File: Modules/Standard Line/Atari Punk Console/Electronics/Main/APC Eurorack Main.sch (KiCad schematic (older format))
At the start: 23 parts, among them IC1 L78L05_TO92, IC2 LM556, J1 Power, J4 CV2, J5 Out, J6 CV1

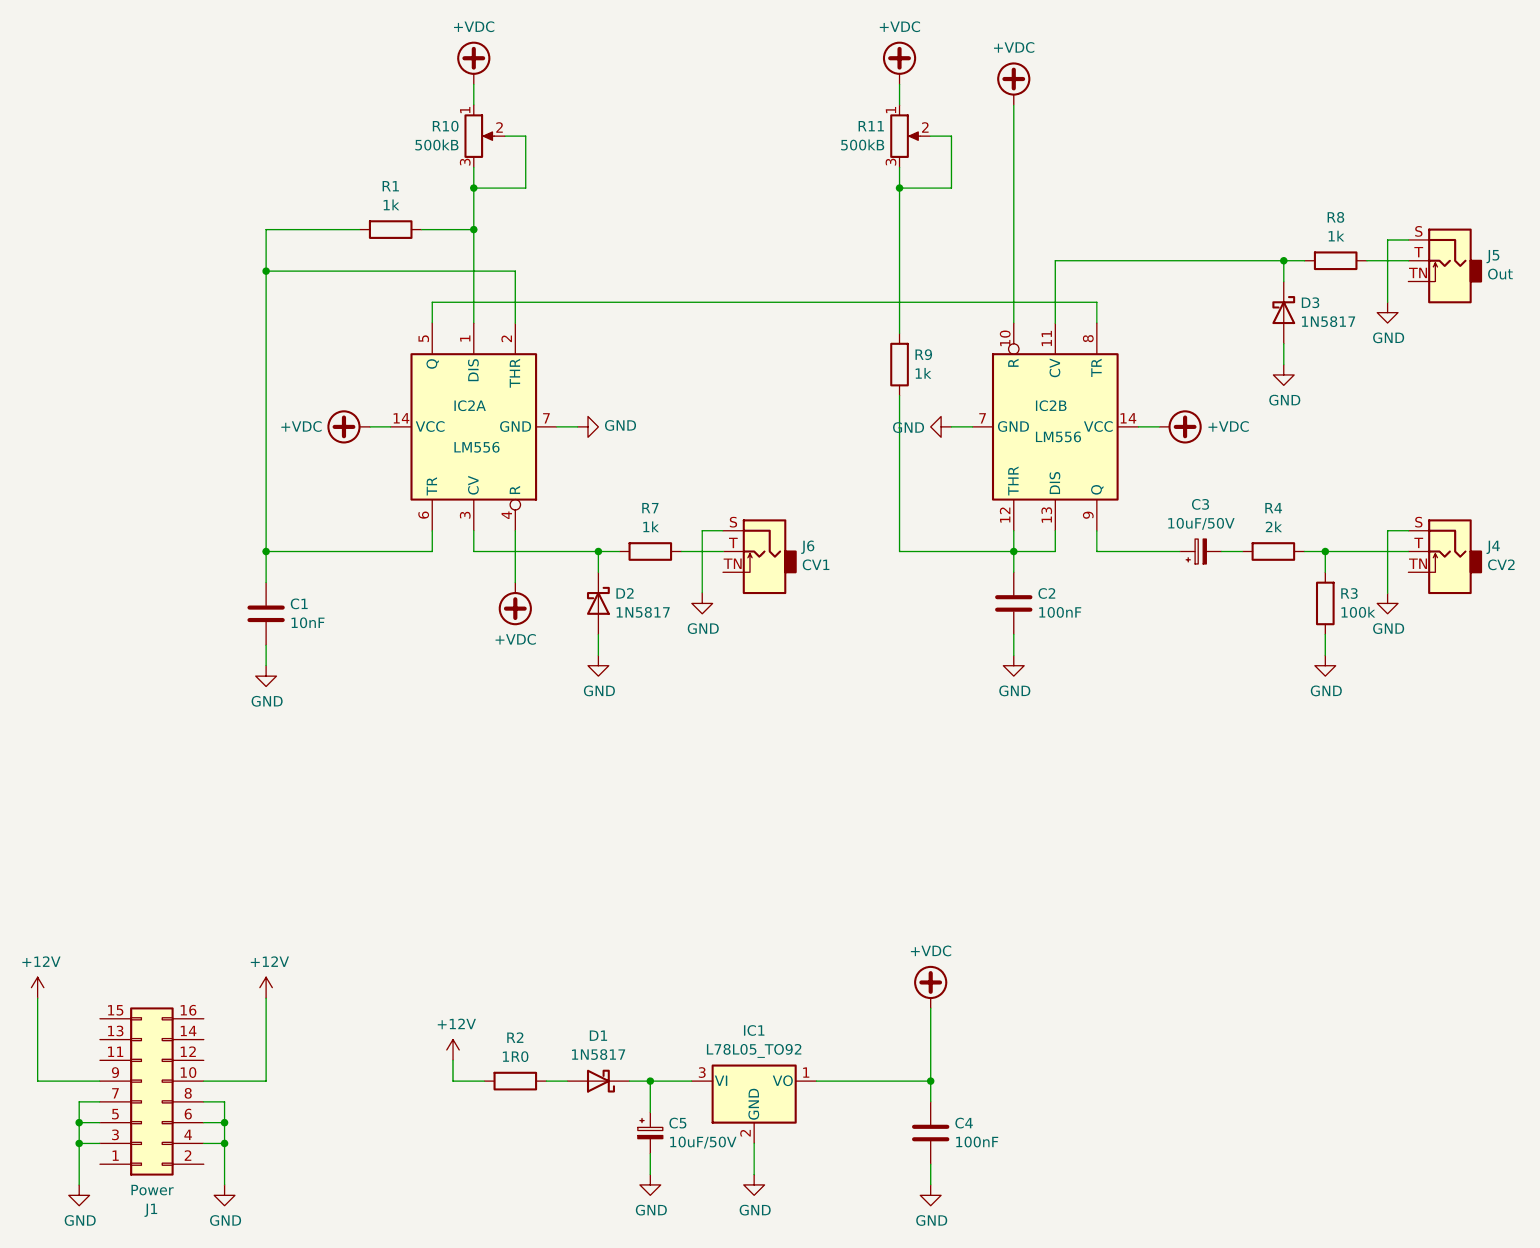
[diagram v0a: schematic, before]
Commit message: 4Ch Mixer added
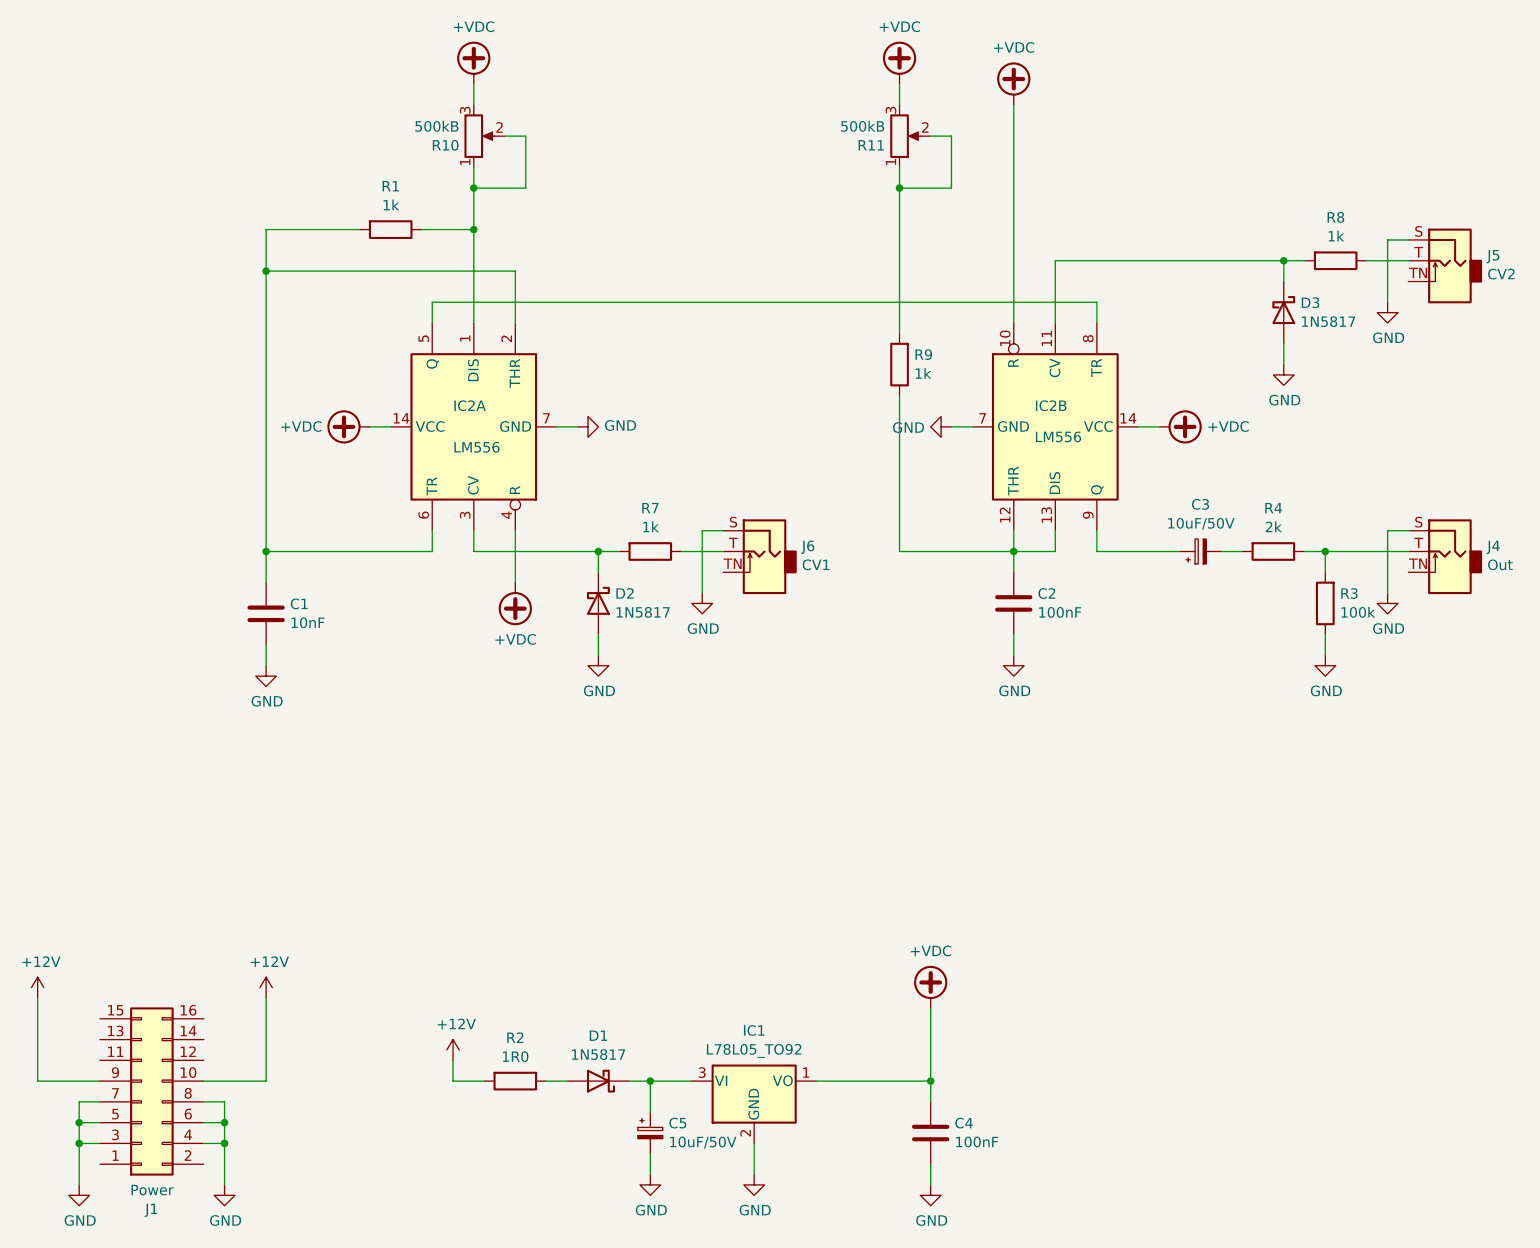
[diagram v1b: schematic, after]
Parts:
- J4: value CV2 -> Out
- J5: value Out -> CV2
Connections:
- net +VDC: now also R10.3, R11.3; no longer R10.1, R11.1
- net at IC2.1 (DIS), R1.1, R10.2: now also R10.1; no longer R10.3
- net at R11.2, R9.2: now also R11.1; no longer R11.3
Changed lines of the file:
@@
 F 3 "~" H 3150 2150 50  0001 C CNN
 	1    3150 2150
-	1    0    0    -1
+	1    0    0    1
 $EndComp
 $Comp
@@
 F 3 "~" H 5200 2150 50  0001 C CNN
 	1    5200 2150
-	1    0    0    -1
+	1    0    0    1
 $EndComp
 $Comp
@@
 P 7850 4150
 F 0 "J4" H 7670 4175 50  0000 R CNN
-F 1 "CV2" H 7670 4084 50  0000 R CNN
+F 1 "Out" H 7670 4084 50  0000 R CNN
 F 2 "Connector_Audio_PJSeries:PJ-323" H 7850 4150 50  0001 C CNN
 F 3 "~" H 7850 4150 50  0001 C CNN
@@
 P 7850 2750
 F 0 "J5" H 7670 2775 50  0000 R CNN
-F 1 "Out" H 7670 2684 50  0000 R CNN
+F 1 "CV2" H 7670 2684 50  0000 R CNN
 F 2 "Connector_Audio_PJSeries:PJ-323" H 7850 2750 50  0001 C CNN
 F 3 "~" H 7850 2750 50  0001 C CNN
